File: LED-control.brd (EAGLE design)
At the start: 48.3 x 48.3 mm, 32 parts

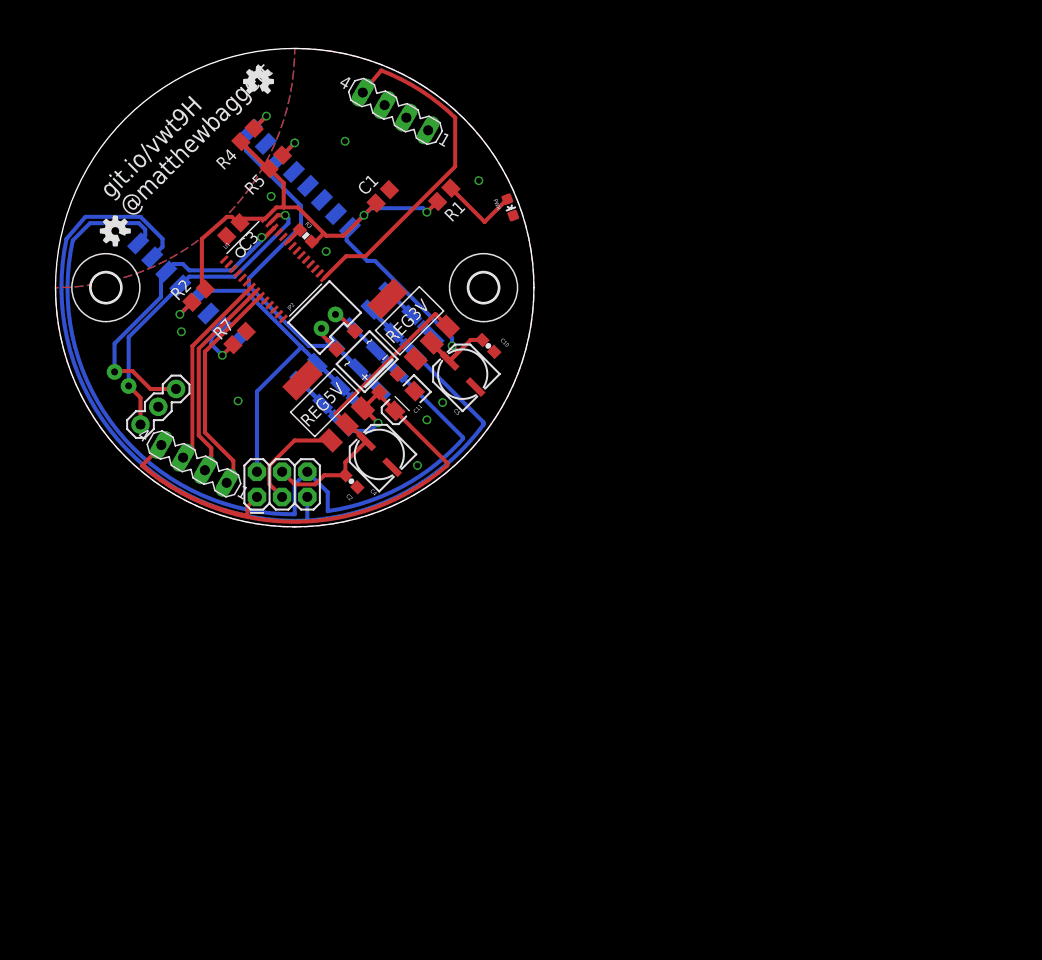
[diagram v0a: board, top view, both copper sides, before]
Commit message: Reworking board to standardise on 1206 caps and resistors. Moving caps into the center where they'll clip through the hole in the top board. Move power connector to rear (duh). Remove i2c connectors. Replace programming harness connector with better one, with i2c. Add i2c pullups.
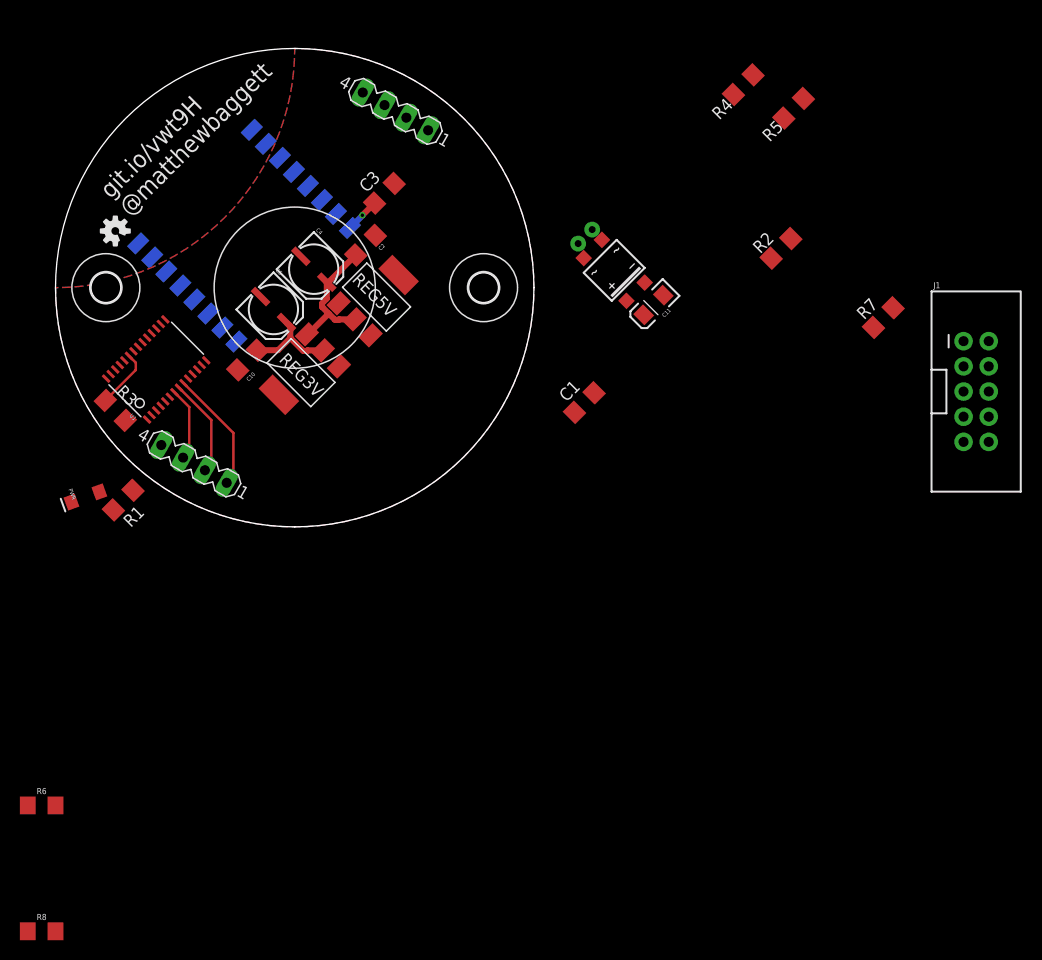
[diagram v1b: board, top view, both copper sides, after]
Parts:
- removed I2C1: (no value), SparkFun-Connectors:JST-2-PTH-NS
- removed JP1: (no value), SparkFun-Connectors:1X06_SMD_STRAIGHT_COMBO
- removed JP3: (no value), SparkFun-Connectors:1X06-SMD_EDGE
- removed JP4: FEMALE 2x3, SparkFun-Connectors:2X3
- removed JP5: (no value), SparkFun-Connectors:1X03
- removed LOGO2: OSHW-LOGOS, SparkFun-Aesthetics:OSHW-LOGO-S
- added J1: (no value), SparkFun-Connectors:2X5-SHROUDED
- added R6, R8: (no value), SparkFun-Resistors:1206
- C1, C3: device rcl:C0805 -> rcl:C1206
- C10, C2: device SparkFun-Capacitors:0603-CAP -> rcl:C1206
- PWR: value red -> RED; device SparkFun-LED:LED-0603 -> SparkFun-LED:LED-1206
- R1: value 330Ohm -> (none); device rcl:R0805 -> SparkFun-Resistors:1206
- R2, R4, R5, R7: value 10k -> (none); device rcl:R0805 -> SparkFun-Resistors:1206
- R3: value (none) -> (none); device SparkFun-Resistors:0603-RES -> rcl:R1206
- moved R7 65.0 mm to (83.5, 21.1)
- moved R2 58.9 mm to (73.2, 28.1)
- moved R5 52.5 mm to (74.5, 42.2)
- moved PWR 51.9 mm to (3.02, 3.02)
- moved R4 50.3 mm to (69.4, 44.6)
- moved R1 44.7 mm to (6.83, 2.70)
- moved C1 29.1 mm to (53.3, 12.5)
- moved JP2 27.8 mm to (53.8, 28.9), flipped to the bottom, turned to 135 degrees
- moved C11 26.9 mm to (60.3, 22.4)
- moved B1 26.6 mm to (56.4, 25.9)
- moved R3 26.1 mm to (6.03, 11.7)
- moved C10 24.3 mm to (19.4, 16.8), turned to 225 degrees
- moved C2 23.9 mm to (31.3, 28.4), turned to 45 degrees
- moved C5 20.1 mm to (22.1, 22.1), turned to 315 degrees
- moved C4 20.1 mm to (26.2, 26.2), turned to 315 degrees
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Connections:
- net +5V: now also J1.6; no longer JP4.4
- net 12V: now also J1.1; no longer JP1.6, JP3.6, JP4.1
- net 3.3V: now also R6.1, R8.1; no longer R3.2
- net GND: now also J1.5, R3.2; no longer JP1.1, JP3.1, JP4.3, JP5.2
- net GPIO0: now also J1.4; no longer JP1.5, JP3.5, JP4.2
- net RESET: now also J1.2; no longer JP1.4, JP3.4
- net RX: now also J1.10; no longer JP1.2, JP3.2, JP4.5
- net SCL: now also J1.7, R8.2; no longer I2C1.1, JP5.3
- net SDA: now also J1.9, R6.2; no longer I2C1.2, JP5.1
- net TX: now also J1.8; no longer JP1.3, JP3.3, JP4.6
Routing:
- net RX: track 90.2 -> 0.00 mm
- net TX: track 83.2 -> 0.00 mm
- net 12V: track 72.8 -> 0.00 mm, vias 1 -> 0
- net 3.3V: track 76.0 -> 13.0 mm, vias 3 -> 1
- net RESET: track 41.5 -> 0.00 mm, vias 1 -> 0
- net GPIO0: track 40.1 -> 0.00 mm, vias 1 -> 0
- net WHITE: track 34.5 -> 0.00 mm
- net SDA: track 33.0 -> 0.00 mm, vias 1 -> 0
- net SCL: track 32.7 -> 0.00 mm, vias 1 -> 0
- net +5V: track 31.8 -> 13.7 mm
- net BLUE: track 20.1 -> 7.48 mm
- net RED: track 21.2 -> 9.95 mm
- net GND: track 10.9 -> 0.00 mm, vias 9 -> 0
- net GREEN: track 22.6 -> 12.4 mm
- net N$2: track 8.06 -> 0.00 mm
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
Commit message: Finalised board design
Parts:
- removed J1: (no value), SparkFun-Connectors:2X5-SHROUDED
- added J2: (no value), SparkFun-Connectors:2X5-SHROUDED
- moved R8 69.1 mm to (11.9, 27.0), turned to 225 degrees
- moved R7 64.0 mm to (19.7, 26.4)
- moved R2 57.4 mm to (16.0, 22.7)
- moved R6 55.2 mm to (13.9, 24.9), turned to 225 degrees
- moved PWR 51.7 mm to (45.7, 32.2), turned to 290 degrees
- moved C1 49.5 mm to (4.13, 17.6)
- moved R1 47.2 mm to (42.1, 34.1), turned to 110 degrees
- moved R5 47.2 mm to (27.3, 40.5), turned to 225 degrees
- moved R4 43.9 mm to (25.6, 42.2), turned to 225 degrees
- moved JP2 23.0 mm to (31.8, 35.4)
- moved C11 22.5 mm to (38.7, 28.9)
- moved B1 22.4 mm to (34.9, 32.4)
- moved C3 5.34 mm to (28.6, 31.0), turned to 135 degrees
- moved R3 1.35 mm to (6.99, 10.8)
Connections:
- net +5V: now also J2.7; no longer J1.6
- net 12V: now also J2.9; no longer J1.1
- net 3.3V: now also J2.5
- net GND: now also J2.6; no longer J1.5
- net GPIO0: now also J2.8; no longer J1.4
- net RESET: now also J2.10; no longer J1.2
- net RX: now also J2.4; no longer J1.10
- net SCL: now also J2.1; no longer J1.7
- net SDA: now also J2.3; no longer J1.9
- net TX: now also J2.2; no longer J1.8
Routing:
- net 3.3V: track 13.0 -> 123.1 mm
- net WHITE: track 0.00 -> 64.0 mm, vias 0 -> 2
- net 12V: track 0.00 -> 63.8 mm
- net SDA: track 0.00 -> 48.6 mm, vias 0 -> 1
- net RESET: track 0.00 -> 39.4 mm, vias 0 -> 1
- net SCL: track 0.00 -> 39.1 mm, vias 0 -> 1
- net RX: track 0.00 -> 33.7 mm
- net TX: track 0.00 -> 33.4 mm
- net GPIO0: track 0.00 -> 29.9 mm, vias 0 -> 1
- net +5V: track 13.7 -> 22.7 mm
- net GPIO15: track 0.00 -> 6.03 mm, vias 0 -> 1
- net CH_PD: track 0.00 -> 4.63 mm, vias 0 -> 1
- net N$2: track 0.00 -> 2.78 mm
- net N$3: track 0.00 -> 2.05 mm
- net N$4: track 0.00 -> 1.96 mm
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
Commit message: mk10
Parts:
- added R9: 470, SparkFun-Resistors:1206
- R2, R4, R5, R6, R7, R8: value (none) -> 10k
- moved R4 0.45 mm to (25.2, 42.5)
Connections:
- net GPIO16: now also R9.1
- net RESET: now also R9.2
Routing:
- net RESET: track 39.4 -> 48.2 mm, vias 1 -> 2
- net GPIO16: track 0.00 -> 7.89 mm, vias 0 -> 1
- net WHITE: track 64.0 -> 64.9 mm
- net 3.3V: track 123.1 -> 122.7 mm, vias 1 -> 0
